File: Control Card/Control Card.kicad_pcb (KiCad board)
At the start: 2 copper layers, 233 x 160 mm, 38 parts, among them U1 CY7C1021D, U10 74ACT273, U100 74LVC1G08, U101 74LVC1G32, U102 74LVC2G157, U11 74ACT151, U110 74ACT244, U111 74ACT374, U112 74ACT374, U113 74ACT374, U114 74ACT374, U115 74ACT374, U116 74ACT374, U117 74ACT374, U118 74ACT374, U119 74ACT374, U12 74ACT86, U13 74ACT32, U14 74ACT04, U15 74ACT153, U16 74ACT153, U17 74ACT153, U18 74ACT153, U2 CY7C1021D, U20 74ACT02, U21 74ACT20, U24 74ACT30, U3 CY7C1021D, U44 74ACT11, U5 74ACT273, U53 74ACT04, U6 74ACT273, U61 74ACT32, U7 74ACT273, U8 74ACT273, U9 74ACT273

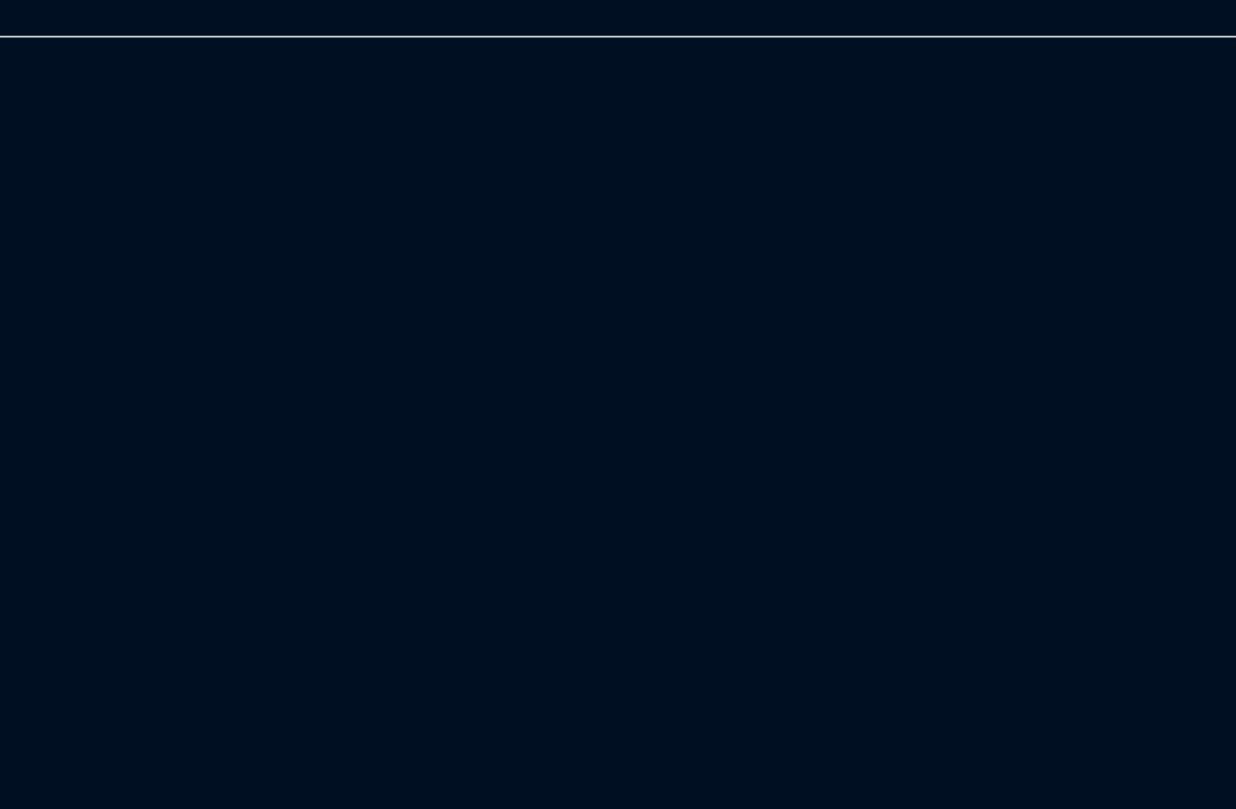
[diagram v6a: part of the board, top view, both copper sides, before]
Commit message: add an ESP32 as a service processor
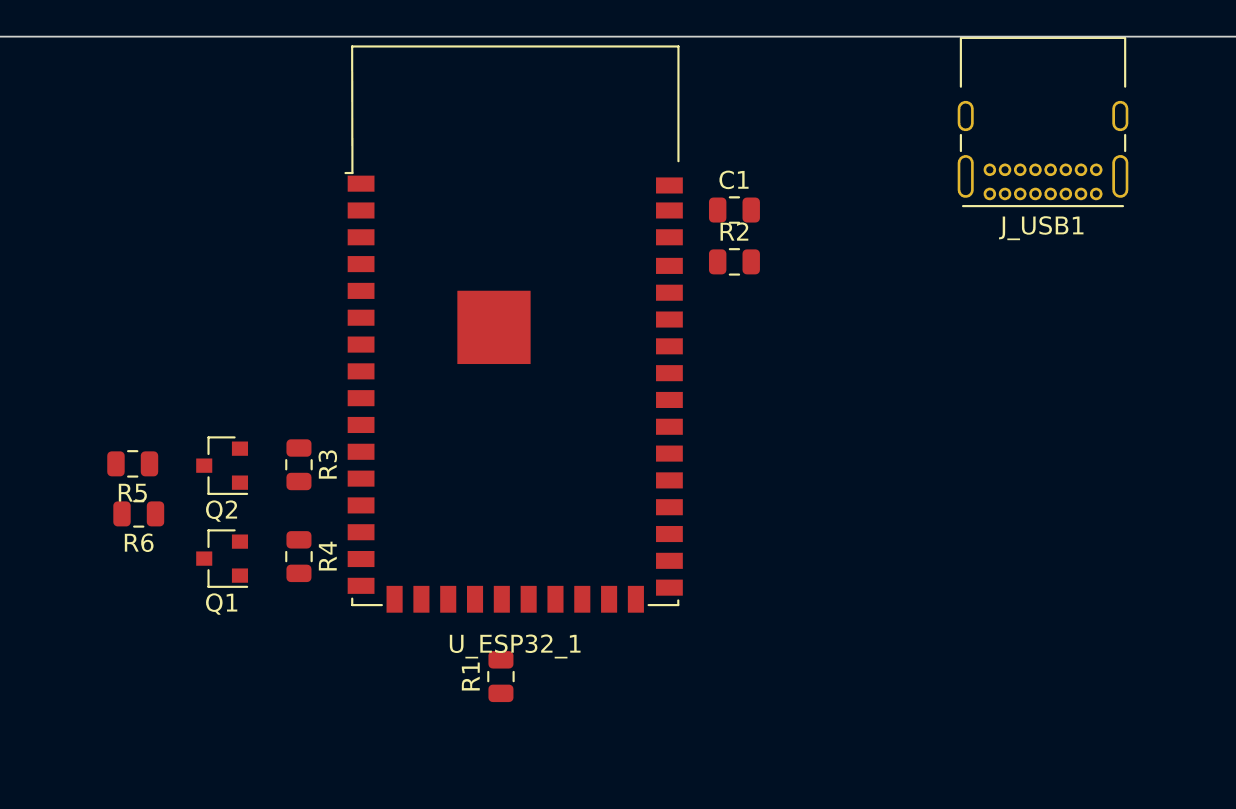
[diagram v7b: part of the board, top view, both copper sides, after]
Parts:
- added C1: 0.1µF, Capacitor_SMD:C_0805_2012Metric, F.Cu at (91.3, 34.7)
- added J_USB1: USB_C_Receptacle_USB2.0, Connector_USB:USB_C_Receptacle_GCT_USB4085, F.Cu at (111.5, 33.8)
- added Q1: 2N7002, Package_TO_SOT_SMD:SOT-23, F.Cu at (62.6, 54.2)
- added Q2: 2N7002, Package_TO_SOT_SMD:SOT-23, F.Cu at (62.6, 49.0)
- added R1: 10kΩ, Resistor_SMD:R_0805_2012Metric, F.Cu at (78.2, 60.8)
- added R2: 10kΩ, Resistor_SMD:R_0805_2012Metric, F.Cu at (91.3, 37.6)
- added R3: 2.2kΩ, Resistor_SMD:R_0805_2012Metric, F.Cu at (66.9, 49.0)
- added R4: 2.2kΩ, Resistor_SMD:R_0805_2012Metric, F.Cu at (66.9, 54.1)
- added R5: 2.2kΩ, Resistor_SMD:R_0805_2012Metric, F.Cu at (57.6, 48.9)
- added R6: 2.2kΩ, Resistor_SMD:R_0805_2012Metric, F.Cu at (57.9, 51.7)
- added U_ESP32_1: ESP32-S2-WROVER-I, RF_Module:ESP32-S2-WROVER, F.Cu at (79.0, 45.0)
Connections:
- net VCC renamed +5V
- U10 pad 17: /Microcode/io_RUSER_PTB -> Net-(U10-Pad17)
- U10 pad 8: /Microcode/io_USE_CARRY -> Net-(U10-Pad8)
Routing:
- added copper zone on In1.Cu, net +5V
- added copper zone on In2.Cu, net GND
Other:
- copper layers 2 -> 4

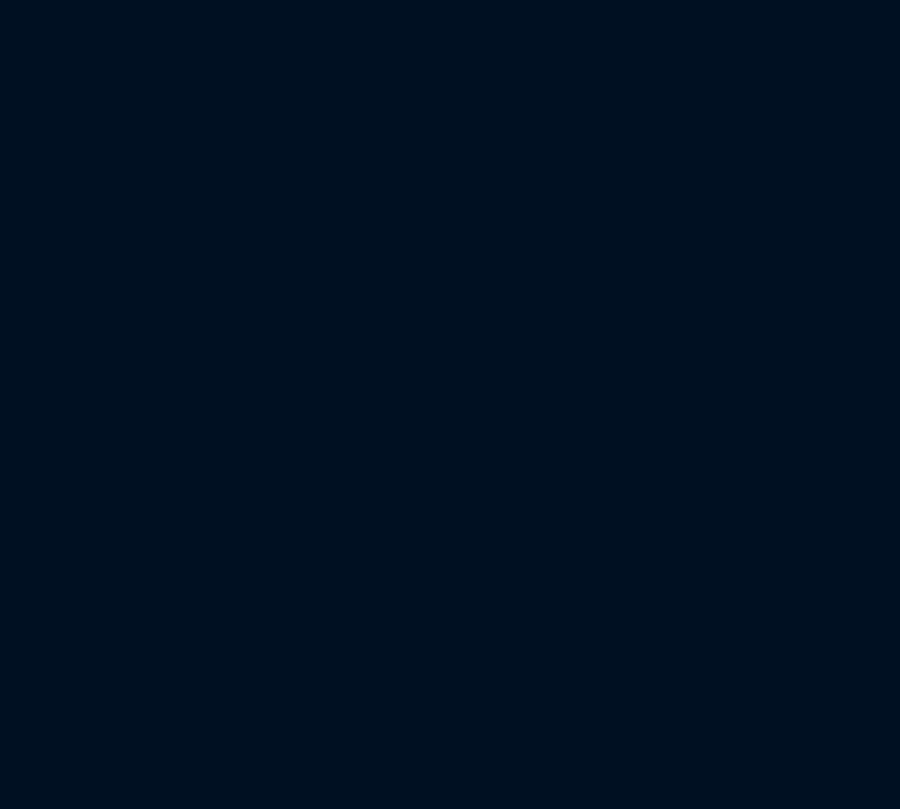
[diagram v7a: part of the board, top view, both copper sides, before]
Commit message: add lots of nets to the Din connectors
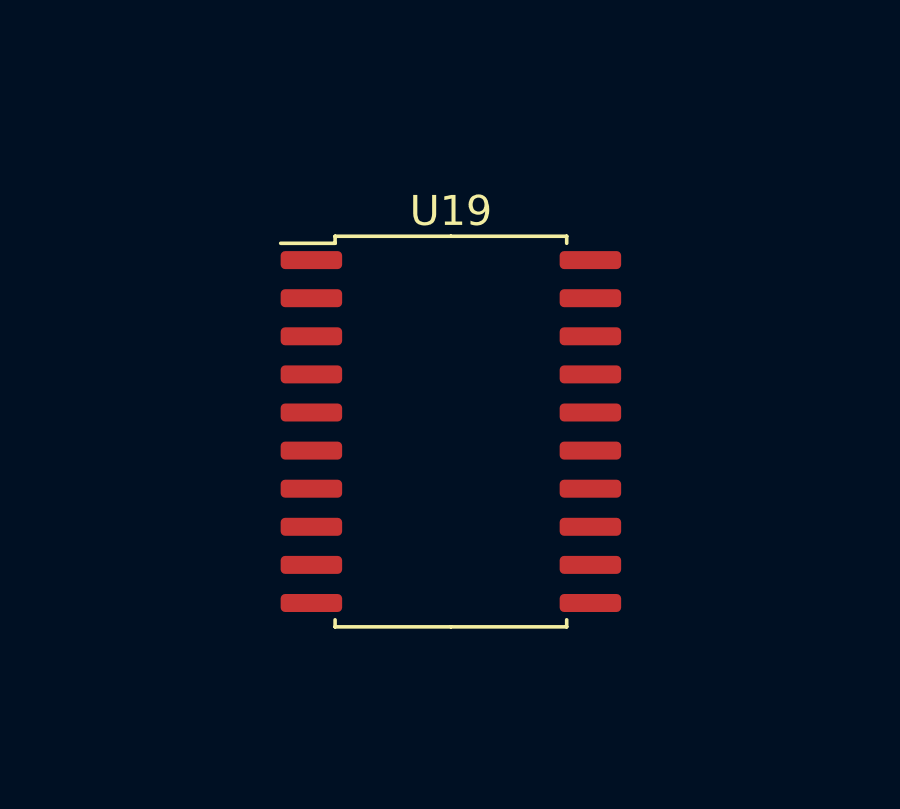
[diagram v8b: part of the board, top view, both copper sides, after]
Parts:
- added U19: 74ACT273, Package_SO:SOIC-20W_7.5x12.8mm_P1.27mm, F.Cu at (64.2, 95.9)
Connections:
- net Net-(J_LEFT1-Padb10) renamed MEMREF
- net Net-(J_LEFT1-Padb14) renamed ~RESET~
- net Net-(J_LEFT1-Padb15) renamed ~STOP_CLK~
- net Net-(J_LEFT1-Padb16) renamed ~WR~
- net Net-(J_LEFT1-Padb18) renamed XL_MDR_HI
- net Net-(J_LEFT1-Padb19) renamed XL_MDR_LO
- net Net-(J_LEFT1-Padb2) renamed MEMORY
- net Net-(J_LEFT1-Padb25) renamed ~RD~
- net Net-(J_LEFT1-Padb26) renamed ~IRQ4~
- net Net-(J_LEFT1-Padb6) renamed ~PSEL_1~
- net Net-(J_RIGHT1-Pada1) renamed ALUOP0
- net Net-(J_RIGHT1-Pada10) renamed CLKS
- net Net-(J_RIGHT1-Pada12) renamed ~ER_MDR~
- net Net-(J_RIGHT1-Pada13) renamed ~ER_IMM~
- net Net-(J_RIGHT1-Pada14) renamed ~HALT~
- net Net-(J_RIGHT1-Pada16) renamed CLKM
- net Net-(J_RIGHT1-Pada18) renamed XINIT_INST
- net Net-(J_RIGHT1-Pada2) renamed ALUOP1
- net Net-(J_RIGHT1-Pada20) renamed L_PC
- net Net-(J_RIGHT1-Pada21) renamed ~EL_MAR~
- net Net-(J_RIGHT1-Pada22) renamed ~EL_C~
- net Net-(J_RIGHT1-Pada23) renamed ~EL_PC~
- net Net-(J_RIGHT1-Pada24) renamed ~EL_DP~
- net Net-(J_RIGHT1-Pada25) renamed ~EL_SP~
- net Net-(J_RIGHT1-Pada26) renamed ~EL_A~
- net Net-(J_RIGHT1-Pada27) renamed ~EL_B~
- net Net-(J_RIGHT1-Pada28) renamed ~EL_MDR~
- net Net-(J_RIGHT1-Pada29) renamed ~EL_SSP~
- net Net-(J_RIGHT1-Pada3) renamed USE_CARRY
- net Net-(J_RIGHT1-Pada30) renamed ~EL_TPC~
- net Net-(J_RIGHT1-Pada31) renamed ~EL_MSW~
- net Net-(J_RIGHT1-Pada32) renamed xCODE_PTB
- net Net-(J_RIGHT1-Pada4) renamed ALUOP_SZ
- net Net-(J_RIGHT1-Pada5) renamed IMMVAL0
- net Net-(J_RIGHT1-Pada6) renamed IMMVAL1
- net Net-(J_RIGHT1-Pada7) renamed L_EI
- net Net-(J_RIGHT1-Pada8) renamed L_PTB
- net Net-(J_RIGHT1-Padb10) renamed L_C
- net Net-(J_RIGHT1-Padb14) renamed L_DP
- net Net-(J_RIGHT1-Padb15) renamed L_SSP
- net Net-(J_RIGHT1-Padb16) renamed ~L_PTE~
- net Net-(J_RIGHT1-Padb18) renamed MSWP
- net Net-(J_RIGHT1-Padb19) renamed MSWE
- net Net-(J_RIGHT1-Padb26) renamed MSWM
- net Net-(J_RIGHT1-Padb3) renamed L_MODE
- net Net-(J_RIGHT1-Padb4) renamed L_PAGING
- net Net-(J_RIGHT1-Padb5) renamed L_MAR
- net Net-(J_RIGHT1-Padb7) renamed L_MDR_LO
- net Net-(J_RIGHT1-Padb8) renamed L_MDR_HI
- net Net-(J_RIGHT1-Padb9) renamed L_MSW
- net Net-(J_RIGHT1-Padc1) renamed ~NP~
- net Net-(J_RIGHT1-Padc10) renamed ~E_MDR_LO~
- net Net-(J_RIGHT1-Padc11) renamed ~E_MDR_HI~
- net Net-(J_RIGHT1-Padc12) renamed ~IRQ0~
- net Net-(J_RIGHT1-Padc13) renamed ~IRQ1~
- net Net-(J_RIGHT1-Padc14) renamed ~IRQ2~
- net Net-(J_RIGHT1-Padc15) renamed ~IRQ3~
- net Net-(J_RIGHT1-Padc16) renamed USER_PTB
- net Net-(J_RIGHT1-Padc17) renamed ~IRQ5~
- net Net-(J_RIGHT1-Padc18) renamed L_B_HI
- net Net-(J_RIGHT1-Padc19) renamed L_B_LO
- net Net-(J_RIGHT1-Padc2) renamed ~NW~
- net Net-(J_RIGHT1-Padc20) renamed ~DMA_ACK~
- net Net-(J_RIGHT1-Padc21) renamed FP_L0
- net Net-(J_RIGHT1-Padc22) renamed FP_L1
- net Net-(J_RIGHT1-Padc23) renamed FP_L2
- net Net-(J_RIGHT1-Padc24) renamed FP_L3
- net Net-(J_RIGHT1-Padc25) renamed ~RW~
- net Net-(J_RIGHT1-Padc26) renamed ~WAIT~
- net Net-(J_RIGHT1-Padc27) renamed ~E_PTE~
- net Net-(J_RIGHT1-Padc28) renamed ~FP_WRITE~
- net Net-(J_RIGHT1-Padc29) renamed ~DMA_REQ~
- net Net-(J_RIGHT1-Padc3) renamed L_SP
- net Net-(J_RIGHT1-Padc30) renamed ~SET_FLAGS~
- net Net-(J_RIGHT1-Padc31) renamed L_FPL
- net Net-(J_RIGHT1-Padc32) renamed CODE_PTB
- net Net-(J_RIGHT1-Padc4) renamed COMMIT
- net Net-(J_RIGHT1-Padc5) renamed L_A_HI
- net Net-(J_RIGHT1-Padc6) renamed L_A_LO
- net Net-(J_RIGHT1-Padc7) renamed ~DO_RSHIFT~
- net Net-(J_RIGHT1-Padc8) renamed L_FAULT
- J_LEFT1 pad b28: Net-(J_LEFT1-Padb28) -> IR1
- J_LEFT1 pad b29: Net-(J_LEFT1-Padb29) -> IR2
- J_LEFT1 pad b30: Net-(J_LEFT1-Padb30) -> IR3
- J_RIGHT1 pad b25: Net-(J_RIGHT1-Padb25) -> MSWV
- J_RIGHT1 pad b28: Net-(J_RIGHT1-Padb28) -> MSWS
- J_RIGHT1 pad b29: Net-(J_RIGHT1-Padb29) -> MSWC
- J_RIGHT1 pad b30: Net-(J_RIGHT1-Padb30) -> MSWZ
